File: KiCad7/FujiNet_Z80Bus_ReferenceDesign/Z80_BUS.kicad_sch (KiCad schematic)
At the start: 5 parts, among them J7 HOST SYSTEM HEADER, J8 DIAG-HOST_SYSTEM_BUS

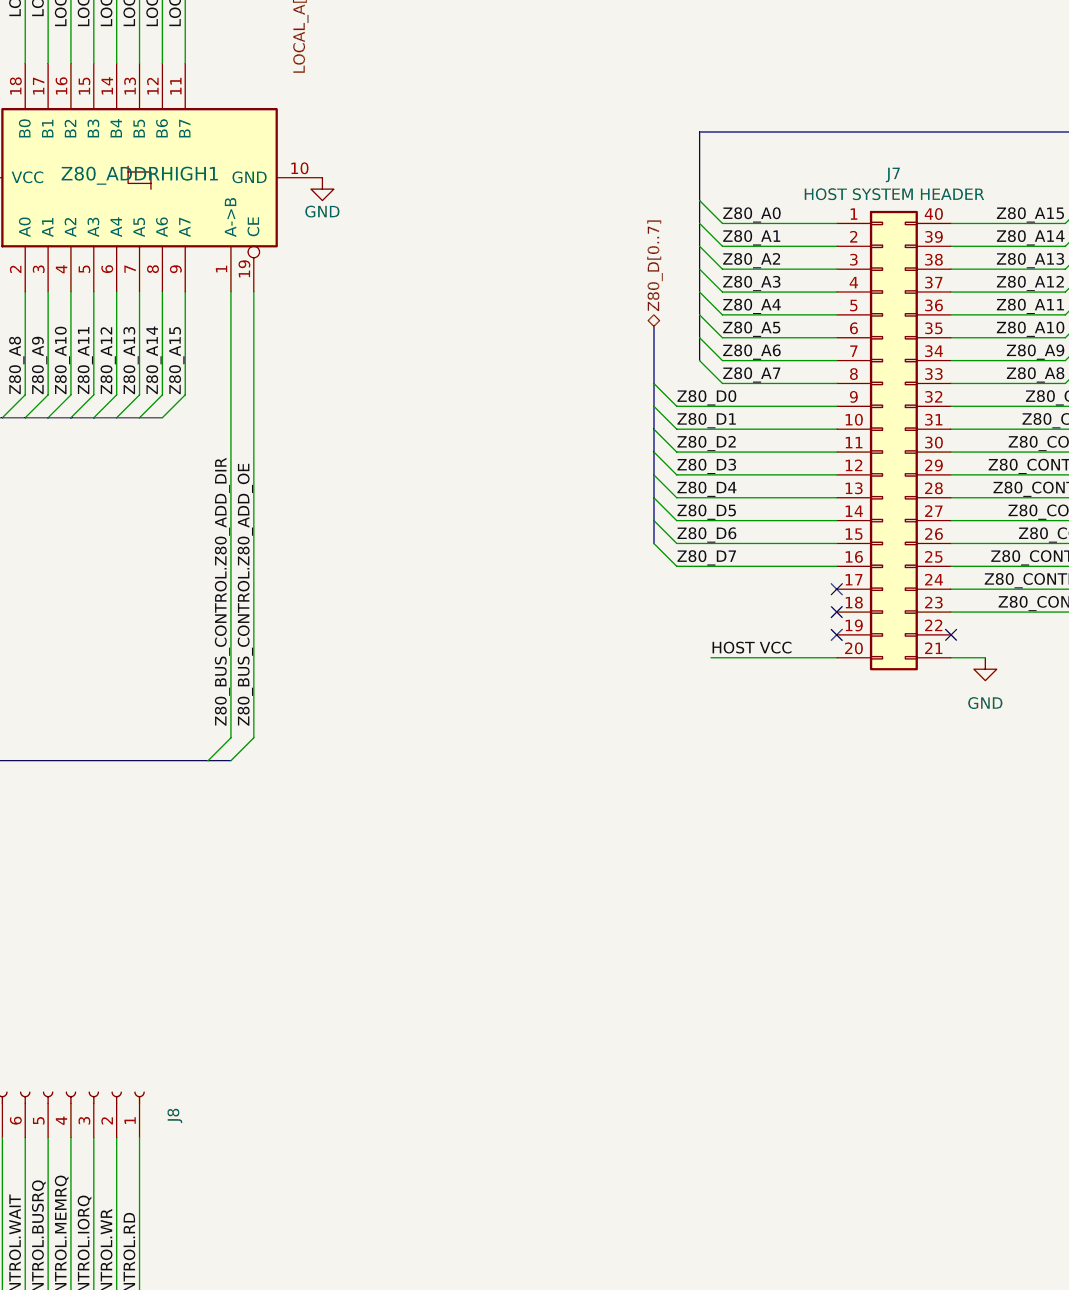
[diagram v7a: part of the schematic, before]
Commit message: KiCad - Fixed Hardlock SET/RESET issue on ERC
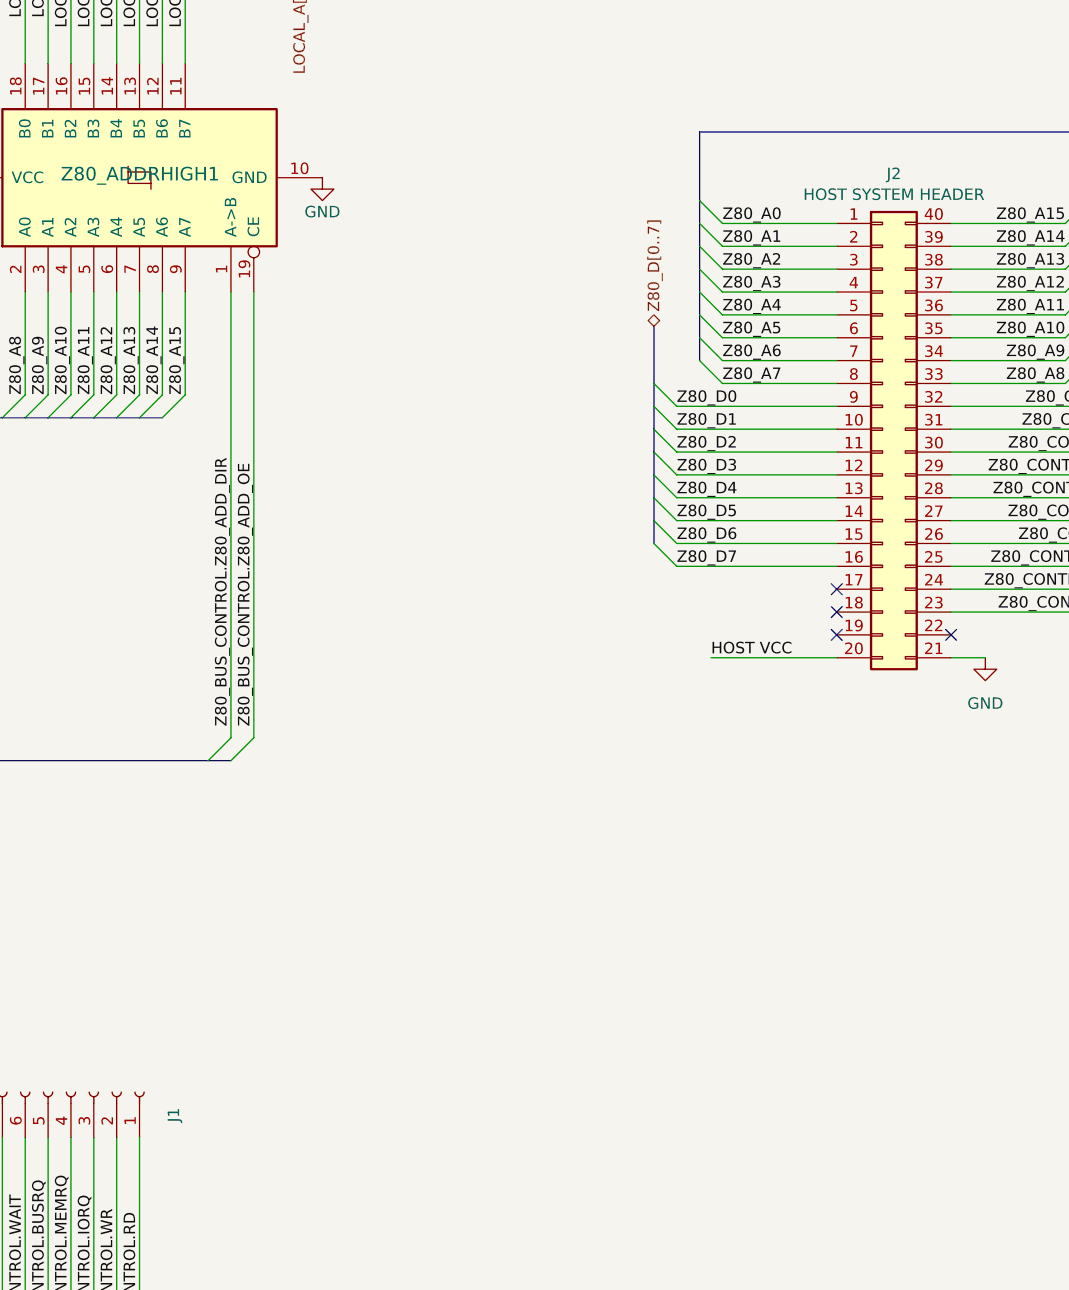
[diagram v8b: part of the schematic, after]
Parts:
- renumbered J8 to J1, J7 to J2
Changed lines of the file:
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@@
   (symbol (lib_id "Connector:Conn_01x40_Socket") (at 100.33 147.32 270) (mirror x) (unit 1)
     (in_bom yes) (on_board yes) (dnp no)
-    (property "Reference" "J8" (at 152.4 149.86 0)
+    (property "Reference" "J1" (at 152.4 149.86 0)
       (effects (font (size 1.27 1.27)))
     )
@@
       (project "FujiNet_Z80Bus_ReferenceDesign"
         (path "/532c0392-800e-45cc-8170-6d32f2390e83/00000000-0000-0000-0000-0000ade3baf4"
-          (reference "J8") (unit 1)
+          (reference "J1") (unit 1)
         )
       )
@@
   (symbol (lib_id "Connector_Generic:Conn_02x20_Counter_Clockwise") (at 231.14 73.66 0) (unit 1)
     (in_bom yes) (on_board yes) (dnp no)
-    (property "Reference" "J7" (at 232.41 45.2882 0)
+    (property "Reference" "J2" (at 232.41 45.2882 0)
       (effects (font (size 1.27 1.27)))
     )
@@
       (project "FujiNet_Z80Bus_ReferenceDesign"
         (path "/532c0392-800e-45cc-8170-6d32f2390e83/00000000-0000-0000-0000-0000ade3baf4"
-          (reference "J7") (unit 1)
+          (reference "J2") (unit 1)
         )
       )
